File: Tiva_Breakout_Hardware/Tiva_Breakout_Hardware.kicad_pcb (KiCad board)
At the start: 2 copper layers, 139.8 x 79.5 mm, 11 parts, among them U1 TM4C129E_Launchpad

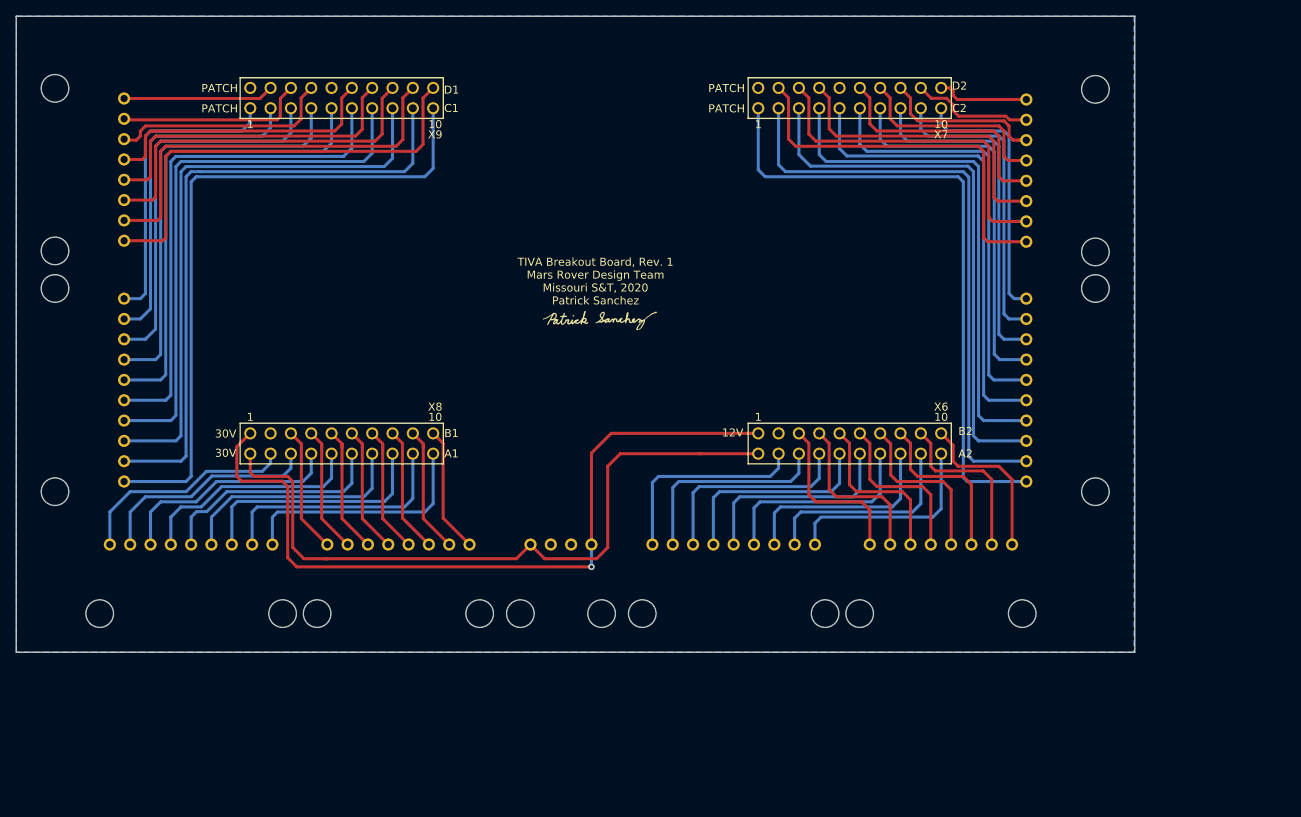
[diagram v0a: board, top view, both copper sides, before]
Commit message: rearranged pcb to account for physical layout
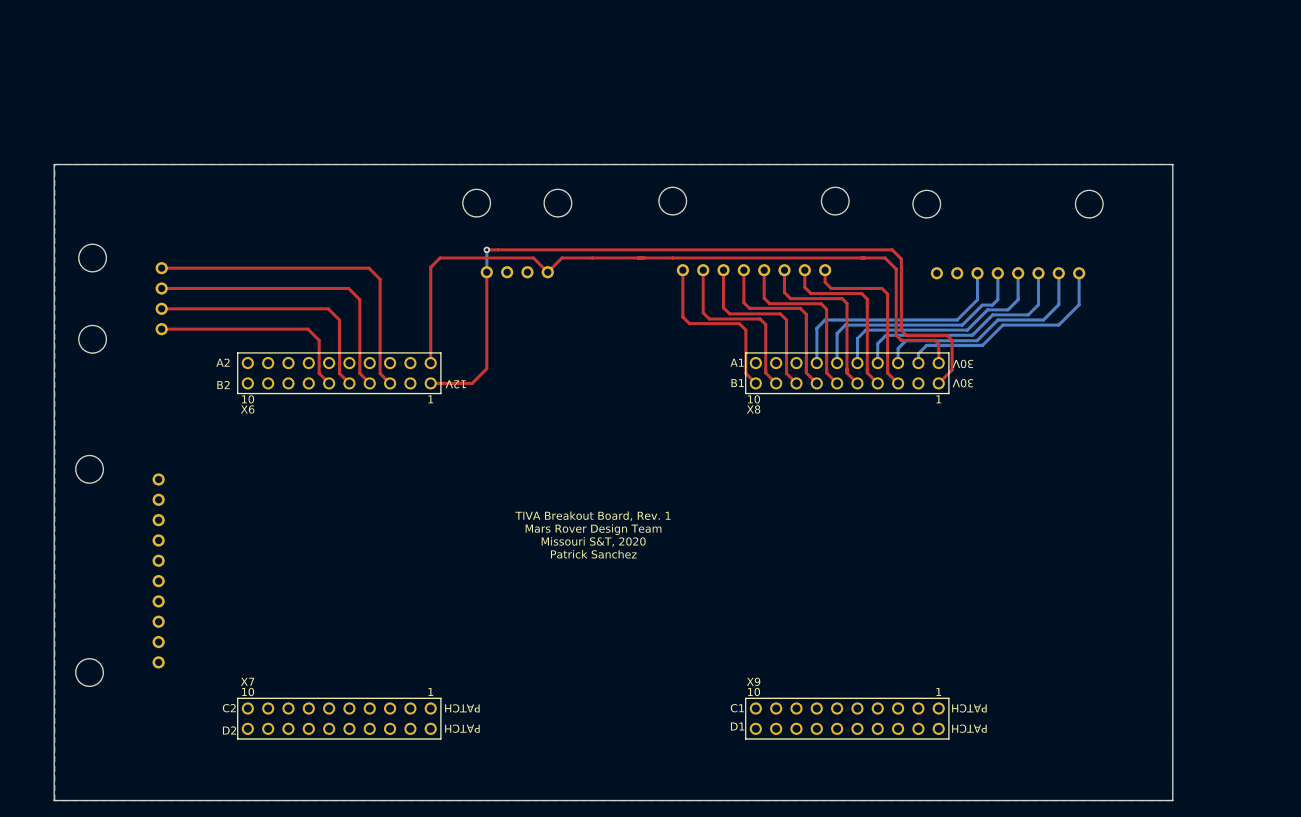
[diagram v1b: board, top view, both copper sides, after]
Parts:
- removed ConnA1, ConnA2: Molex_SL_09, MRDT_Connectors:MOLEX_SL_09_Horizontal
- removed ConnB1, ConnB2, ConnD1, ConnD2: Molex_SL_08, MRDT_Connectors:MOLEX_SL_08_Horizontal
- removed ConnC2: Molex_SL_10, MRDT_Connectors:MOLEX_SL_10_Horizontal
- removed G***: LOGO, MRDT_Silkscreens:z_sig_Patrick_Sanchez_15mmx5mm
- added 12V_B2: Molex_SL_04, MRDT_Connectors:MOLEX_SL_04_Horizontal, B.Cu at (90.3, 87.6)
- added Conn30V_L1: Molex_SL_08, MRDT_Connectors:MOLEX_SL_08_Horizontal, B.Cu at (196.1, 84.5)
- added Conn30V_R1: Molex_SL_08, MRDT_Connectors:MOLEX_SL_08_Horizontal, B.Cu at (164.3, 84.1)
- moved U1 89.7 mm to (188.7, 94.4), turned to 180 degrees
- moved ConnIN1 34.5 mm to (134.7, 84.3), turned to 180 degrees
- moved ConnPCH_C2 23.0 mm to (89.9, 121.7)
- renumbered ConnC1 to ConnPCH_C2
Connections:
- ConnPCH_C2 pad 1: Net-(ConnC1-Pad1) -> Net-(ConnPCH_C2-Pad1)
- ConnPCH_C2 pad 10: Net-(ConnC1-Pad10) -> Net-(ConnPCH_C2-Pad10)
- ConnPCH_C2 pad 2: Net-(ConnC1-Pad2) -> Net-(ConnPCH_C2-Pad2)
- ConnPCH_C2 pad 3: Net-(ConnC1-Pad3) -> Net-(ConnPCH_C2-Pad3)
- ConnPCH_C2 pad 4: Net-(ConnC1-Pad4) -> Net-(ConnPCH_C2-Pad4)
- ConnPCH_C2 pad 5: Net-(ConnC1-Pad5) -> Net-(ConnPCH_C2-Pad5)
- ConnPCH_C2 pad 6: Net-(ConnC1-Pad6) -> Net-(ConnPCH_C2-Pad6)
- ConnPCH_C2 pad 7: Net-(ConnC1-Pad7) -> Net-(ConnPCH_C2-Pad7)
- ConnPCH_C2 pad 8: Net-(ConnC1-Pad8) -> Net-(ConnPCH_C2-Pad8)
- ConnPCH_C2 pad 9: Net-(ConnC1-Pad9) -> Net-(ConnPCH_C2-Pad9)
- U1 pad PF1: Net-(ConnC1-Pad1) -> Net-(U1-PadPF1)
- U1 pad PF2: Net-(ConnC1-Pad2) -> Net-(U1-PadPF2)
- U1 pad PF3: Net-(ConnC1-Pad3) -> Net-(U1-PadPF3)
- U1 pad PG0: Net-(ConnC1-Pad4) -> Net-(U1-PadPG0)
- U1 pad PG1: Net-(ConnC2-Pad1) -> Net-(ConnPCH_C2-Pad1)
- U1 pad PH0: Net-(ConnC2-Pad7) -> Net-(ConnPCH_C2-Pad7)
- U1 pad PH1: Net-(ConnC2-Pad8) -> Net-(ConnPCH_C2-Pad8)
- U1 pad PK4: Net-(ConnC2-Pad2) -> Net-(ConnPCH_C2-Pad2)
- U1 pad PK5: Net-(ConnC2-Pad3) -> Net-(ConnPCH_C2-Pad3)
- U1 pad PK6: Net-(ConnC2-Pad9) -> Net-(ConnPCH_C2-Pad9)
- U1 pad PK7: Net-(ConnC2-Pad10) -> Net-(ConnPCH_C2-Pad10)
- U1 pad PL0: Net-(ConnC1-Pad7) -> Net-(U1-PadPL0)
- U1 pad PL1: Net-(ConnC1-Pad8) -> Net-(U1-PadPL1)
- U1 pad PL2: Net-(ConnC1-Pad9) -> Net-(U1-PadPL2)
- U1 pad PL3: Net-(ConnC1-Pad10) -> Net-(U1-PadPL3)
- U1 pad PL4: Net-(ConnC1-Pad5) -> Net-(U1-PadPL4)
- U1 pad PL5: Net-(ConnC1-Pad6) -> Net-(U1-PadPL5)
- U1 pad PM0: Net-(ConnC2-Pad4) -> Net-(ConnPCH_C2-Pad4)
- U1 pad PM1: Net-(ConnC2-Pad5) -> Net-(ConnPCH_C2-Pad5)
- U1 pad PM2: Net-(ConnC2-Pad6) -> Net-(ConnPCH_C2-Pad6)
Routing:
- net Net-(ConnC1-Pad10): track 83.9 -> 0.00 mm
- net Net-(ConnC1-Pad9): track 79.0 -> 0.00 mm
- net Net-(ConnC2-Pad1): track 79.0 -> 0.00 mm
- net Net-(ConnC2-Pad2): track 73.8 -> 0.00 mm
- net Net-(ConnC1-Pad8): track 73.8 -> 0.00 mm
- net Net-(ConnC1-Pad7): track 68.7 -> 0.00 mm
- net Net-(ConnC2-Pad3): track 68.4 -> 0.00 mm
- net Net-(ConnC2-Pad4): track 63.7 -> 0.00 mm
- net Net-(ConnC1-Pad6): track 63.6 -> 0.00 mm
- net Net-(ConnC1-Pad5): track 58.5 -> 0.00 mm
- net Net-(ConnC2-Pad5): track 58.5 -> 0.00 mm
- net Net-(U1-PadPP2): track 55.9 -> 0.00 mm
- net Net-(ConnC2-Pad6): track 53.5 -> 0.00 mm
- net Net-(ConnC1-Pad4): track 53.5 -> 0.00 mm
- net Net-(U1-PadPN3): track 50.8 -> 0.00 mm
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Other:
- board text removed: "PA4"
- board text removed: "PA5"
- board text removed: "PA6"
- board text removed: "PA7"
- board text removed: "PATCH PANEL"
- board text removed: "PB2"
- board text removed: "PB3"
- board text removed: "PC4"
- board text removed: "PC5"
- board text removed: "PC6"
- board text removed: "PC7"
- board text removed: "PD0"
- board text removed: "PD1"
- board text removed: "PD2"
- board text removed: "PD3"
- board text removed: "PD4"
- board text removed: "PD5"
- board text removed: "PD7"
- board text removed: "PE0"
- board text removed: "PE1"
- board text removed: "PE2"
- board text removed: "PE3"
- board text removed: "PE4"
- board text removed: "PE5"
- board text removed: "PF1"
- board text removed: "PF2"
- board text removed: "PF3"
- board text removed: "PG0"
- board text removed: "PG1"
- board text removed: "PH0"
- board text removed: "PH1"
- board text removed: "PH2"
- board text removed: "PH3"
- board text removed: "PK2"
- board text removed: "PK3"
- board text removed: "PK4"
- board text removed: "PK5"
- board text removed: "PK6"
- board text removed: "PK7"
- board text removed: "PL0"
- board text removed: "PL1"
- board text removed: "PL2"
- board text removed: "PL3"
- board text removed: "PL4"
- board text removed: "PL5"
- board text removed: "PM0"
- board text removed: "PM1"
- board text removed: "PM2"
- board text removed: "PM3"
- board text removed: "PM4"
- board text removed: "PM5"
- board text removed: "PM6"
- board text removed: "PM7"
- board text removed: "PN2"
- board text removed: "PN3"
- board text removed: "PN4"
- board text removed: "PN5"
- board text removed: "PP0"
- board text removed: "PP1"
- board text removed: "PP2"
- board text removed: "PP3"
- board text removed: "PP4"
- board text removed: "PP5"
- board text removed: "PQ0"
- board text removed: "PQ1"
- board text removed: "PQ2"
- board text removed: "PQ3"

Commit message: In process of changing layout for smaller board
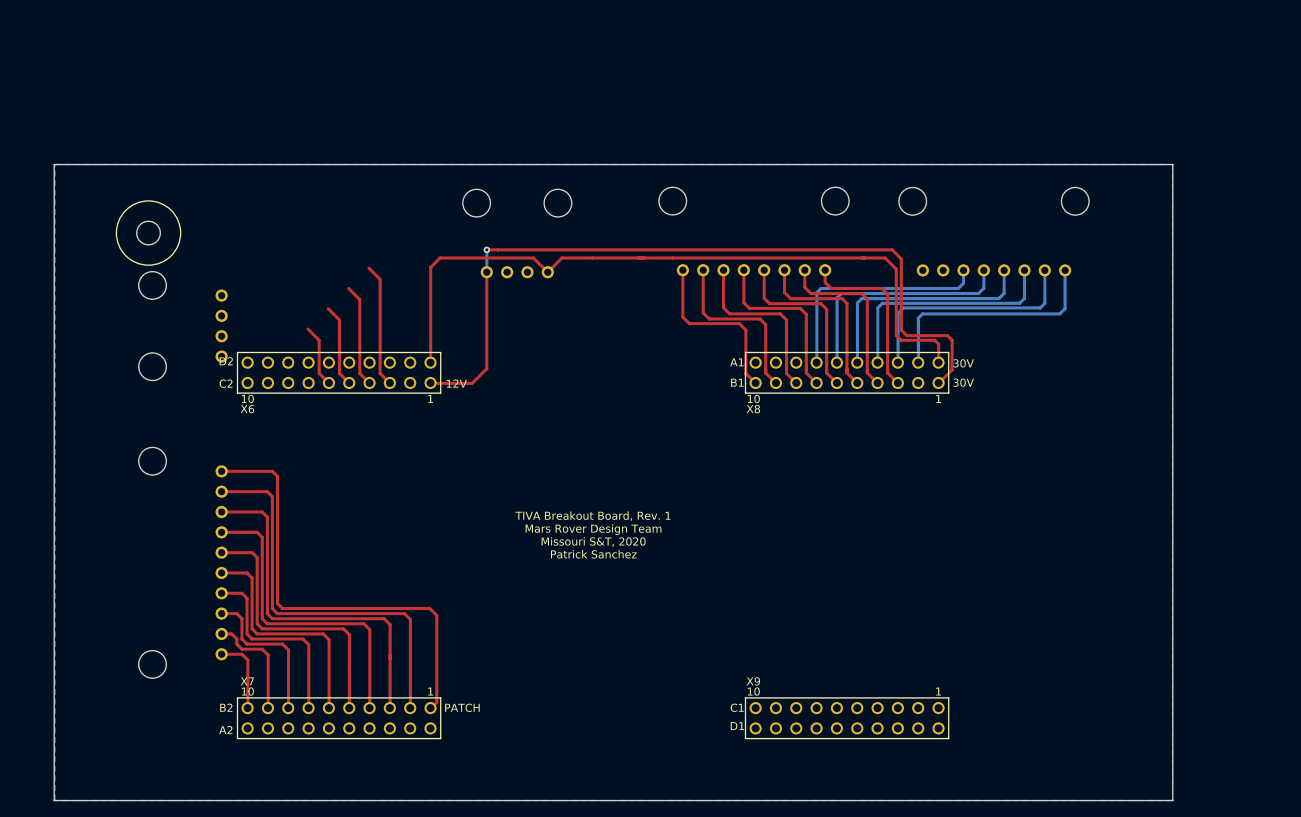
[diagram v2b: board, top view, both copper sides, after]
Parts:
- added REF**: 4_40_Hole, MRDT_Drill_Holes:4_40_Hole_Corner, F.Cu at (92.7, 83.4)
- moved U1 89.2 mm to (107.4, 131.2), turned to 0 degrees
- moved 12V_B2 8.24 mm to (97.8, 91.1)
- moved ConnPCH_C2 7.94 mm to (97.8, 120.7)
- moved Conn30V_L1 1.79 mm to (194.3, 84.1)
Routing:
- net Net-(ConnPCH_C2-Pad1): track 0.00 -> 55.6 mm
- net Net-(ConnPCH_C2-Pad2): track 0.00 -> 49.5 mm
- net Net-(ConnPCH_C2-Pad3): track 0.00 -> 44.9 mm
- net Net-(ConnPCH_C2-Pad4): track 0.00 -> 39.4 mm
- net Net-(ConnPCH_C2-Pad5): track 0.00 -> 34.3 mm
- net Net-(ConnPCH_C2-Pad6): track 0.00 -> 29.2 mm
- net Net-(12V_B2-Pad1): track 41.4 -> 15.5 mm
- net Net-(ConnPCH_C2-Pad7): track 0.00 -> 24.1 mm
- net Net-(12V_B2-Pad2): track 36.3 -> 13.0 mm
- net Net-(12V_B2-Pad3): track 31.5 -> 10.7 mm
- net Net-(ConnPCH_C2-Pad8): track 0.00 -> 19.0 mm
- net Net-(12V_B2-Pad4): track 26.2 -> 7.88 mm
- net Net-(ConnPCH_C2-Pad9): track 0.00 -> 14.0 mm
- net Net-(ConnPCH_C2-Pad10): track 0.00 -> 9.63 mm
- net Net-(Conn30V_L1-Pad1): track 27.9 -> 29.2 mm
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
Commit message: In process of rearranging for new layout
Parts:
- moved 12V_B2 7.50 mm to (104.9, 88.5), turned to 180 degrees
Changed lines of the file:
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@@
   )
   (setup
-    (last_trace_width 0.381)
+    (last_trace_width 0.25)
     (user_trace_width 0.254)
     (user_trace_width 0.381)
@@
     (add_net "Net-(U1-PadRese')")
     (add_net "Net-(U1-PadRese)")
+  )
+  (module MRDT_Connectors:MOLEX_SL_08_Horizontal (layer B.Cu)
+    (at 164.338 84.074 180)
+    (fp_text reference Conn30V_R1 (at -7.62 -2.54) (layer B.SilkS) hide
+      (effects (font (size 1 1) (thickness 0.15)) (justify mirror))
+    )
+    (fp_text value Molex_SL_08 (at 0 -2.54) (layer B.Fab)
+      (effects (font (size 1 1) (thickness 0.15)) (justify mirror))
+    )
+    (fp_line (start -10.16 -1.27) (end -10.16 1.27) (layer B.SilkS) (width 0.15))
+    (fp_line (start 10.16 -1.27) (end -10.16 -1.27) (layer B.SilkS) (width 0.15))
+    (fp_line (start 10.16 1.27) (end 10.16 -1.27) (layer B.SilkS) (width 0.15))
+    (fp_line (start 1.27 5.08) (end 1.27 7.62) (layer B.SilkS) (width 0.15))
+    (fp_line (start -1.27 5.08) (end 1.27 5.08) (layer B.SilkS) (width 0.15))
+    (fp_line (start -1.27 7.62) (end -1.27 5.08) (layer B.SilkS) (width 0.15))
+    (fp_line (start -7.62 8.89) (end -7.62 12.7) (layer B.SilkS) (width 0.15))
+    (fp_line (start 7.62 7.62) (end 7.62 13.208) (layer B.SilkS) (width 0.15))
+    (fp_line (start -7.62 7.62) (end 7.62 7.62) (layer B.SilkS) (width 0.15))
+    (fp_line (start -7.62 8.89) (end -7.62 7.62) (layer B.SilkS) (width 0.15))
+    (fp_line (start -12.06 1.27) (end -12.065 1.27) (layer B.SilkS) (width 0.15))
+    (fp_line (start 12.065 1.27) (end 12.065 13.208) (layer B.SilkS) (width 0.15))
+    (fp_line (start -12.065 1.27) (end -12.065 13.208) (layer B.SilkS) (width 0.15))
+    (fp_line (start -12.065 13.208) (end 12.065 13.208) (layer B.SilkS) (width 0.15))
+    (fp_line (start -7.62 13.208) (end -7.62 12.7) (layer B.SilkS) (width 0.15))
+    (fp_line (start -12.065 1.27) (end 12.065 1.27) (layer B.SilkS) (width 0.15))
+    (pad 8 thru_hole circle (at 8.89 0 180) (size 1.524 1.524) (drill 0.9) (layers *.Cu *.Mask)
+      (net 18 "Net-(Conn30V_R1-Pad8)"))
+    (pad 7 thru_hole circle (at 6.35 0 180) (size 1.524 1.524) (drill 0.9) (layers *.Cu *.Mask)
+      (net 19 "Net-(Conn30V_R1-Pad7)"))
+    (pad 6 thru_hole circle (at 3.81 0 180) (size 1.524 1.524) (drill 0.9) (layers *.Cu *.Mask)
+      (net 20 "Net-(Conn30V_R1-Pad6)"))
+    (pad "" np_thru_hole circle (at 10.16 8.636 180) (size 3.45 3.45) (drill 3.45) (layers *.Cu *.Mask))
+    (pad "" np_thru_hole circle (at -10.16 8.636 180) (size 3.45 3.45) (drill 3.45) (layers *.Cu *.Mask))
+    (pad 5 thru_hole circle (at 1.27 0 180) (size 1.524 1.524) (drill 0.9) (layers *.Cu *.Mask)
+      (net 21 "Net-(Conn30V_R1-Pad5)"))
+    (pad 4 thru_hole circle (at -1.27 0 180) (size 1.524 1.524) (drill 0.9) (layers *.Cu *.Mask)
+      (net 22 "Net-(Conn30V_R1-Pad4)"))
+    (pad 3 thru_hole circle (at -3.81 0 180) (size 1.524 1.524) (drill 0.9) (layers *.Cu *.Mask)
+      (net 23 "Net-(Conn30V_R1-Pad3)"))
+    (pad 2 thru_hole circle (at -6.35 0 180) (size 1.524 1.524) (drill 0.9) (layers *.Cu *.Mask)
+      (net 24 "Net-(Conn30V_R1-Pad2)"))
+    (pad 1 thru_hole circle (at -8.89 0 180) (size 1.524 1.524) (drill 0.9) (layers *.Cu *.Mask)
+      (net 25 "Net-(Conn30V_R1-Pad1)"))
+    (model "${MRDT_KICAD_LIBRARIES}/3D Files/MRDT_Connctors/Molex_SL_08_Horizontal.stp"
+      (offset (xyz 11.42999982833862 12.95399980545044 0))
+      (scale (xyz 1 1 1))
+      (rotate (xyz 0 0 180))
+    )
   )
   (module MRDT_Drill_Holes:4_40_Hole_Corner (layer F.Cu)
@@
   )
   (module MRDT_Connectors:MOLEX_SL_04_Horizontal (layer B.Cu)
-    (at 97.79 91.059 270)
-    (fp_text reference 12V_B2 (at -2.54 -2.54 90) (layer B.SilkS) hide
-      (effects (font (size 1 1) (thickness 0.15)) (justify mirror))
-    )
-    (fp_text value Molex_SL_04 (at -0.635 -2.032 90) (layer B.Fab)
+    (at 104.8512 88.519 180)
+    (fp_text reference 12V_B2 (at -2.54 -2.54) (layer B.SilkS) hide
+      (effects (font (size 1 1) (thickness 0.15)) (justify mirror))
+    )
+    (fp_text value Molex_SL_04 (at -0.635 -2.032) (layer B.Fab)
       (effects (font (size 1 1) (thickness 0.15)) (justify mirror))
     )
@@
     (fp_line (start 5.08 1.27) (end 5.08 -1.27) (layer B.SilkS) (width 0.15))
     (fp_line (start -5.08 -1.27) (end -5.08 1.27) (layer B.SilkS) (width 0.15))
-    (pad 1 thru_hole circle (at -3.81 0 270) (size 1.524 1.524) (drill 0.9) (layers *.Cu *.Mask)
+    (pad 1 thru_hole circle (at -3.81 0 180) (size 1.524 1.524) (drill 0.9) (layers *.Cu *.Mask)
       (net 6 "Net-(12V_B2-Pad1)"))
-    (pad 2 thru_hole circle (at -1.27 0 270) (size 1.524 1.524) (drill 0.9) (layers *.Cu *.Mask)
+    (pad 2 thru_hole circle (at -1.27 0 180) (size 1.524 1.524) (drill 0.9) (layers *.Cu *.Mask)
       (net 7 "Net-(12V_B2-Pad2)"))
-    (pad 3 thru_hole circle (at 1.27 0 270) (size 1.524 1.524) (drill 0.9) (layers *.Cu *.Mask)
+    (pad 3 thru_hole circle (at 1.27 0 180) (size 1.524 1.524) (drill 0.9) (layers *.Cu *.Mask)
       (net 8 "Net-(12V_B2-Pad3)"))
-    (pad 4 thru_hole circle (at 3.81 0 270) (size 1.524 1.524) (drill 0.9) (layers *.Cu *.Mask)
+    (pad 4 thru_hole circle (at 3.81 0 180) (size 1.524 1.524) (drill 0.9) (layers *.Cu *.Mask)
       (net 9 "Net-(12V_B2-Pad4)"))
-    (pad "" np_thru_hole circle (at -5.08 8.636 270) (size 3.45 3.45) (drill 3.45) (layers *.Cu *.Mask))
-    (pad "" np_thru_hole circle (at 5.08 8.636 270) (size 3.45 3.45) (drill 3.45) (layers *.Cu *.Mask))
+    (pad "" np_thru_hole circle (at -5.08 8.636 180) (size 3.45 3.45) (drill 3.45) (layers *.Cu *.Mask))
+    (pad "" np_thru_hole circle (at 5.08 8.636 180) (size 3.45 3.45) (drill 3.45) (layers *.Cu *.Mask))
     (model "${MRDT_KICAD_LIBRARIES}/3D Files/MRDT_Connctors/Molex_SL_04_Horizontal.stp"
       (offset (xyz 6.349999904632568 12.95399980545044 0))
@@
     (model "${MRDT_KICAD_LIBRARIES}/3D Files/MRDT_Connctors/Molex_SL_08_Horizontal.stp"
       (offset (xyz 11.42999982833862 12.95399980545044 0))
-      (scale (xyz 1 1 1))
-      (rotate (xyz 0 0 180))
-    )
-  )
-  (module MRDT_Connectors:MOLEX_SL_08_Horizontal (layer B.Cu)
-    (at 164.338 84.074 180)
-    (fp_text reference Conn30V_R1 (at -7.62 -2.54) (layer B.SilkS) hide
-      (effects (font (size 1 1) (thickness 0.15)) (justify mirror))
-    )
-    (fp_text value Molex_SL_08 (at 0 -2.54) (layer B.Fab)
-      (effects (font (size 1 1) (thickness 0.15)) (justify mirror))
-    )
-    (fp_line (start -10.16 -1.27) (end -10.16 1.27) (layer B.SilkS) (width 0.15))
-    (fp_line (start 10.16 -1.27) (end -10.16 -1.27) (layer B.SilkS) (width 0.15))
-    (fp_line (start 10.16 1.27) (end 10.16 -1.27) (layer B.SilkS) (width 0.15))
-    (fp_line (start 1.27 5.08) (end 1.27 7.62) (layer B.SilkS) (width 0.15))
-    (fp_line (start -1.27 5.08) (end 1.27 5.08) (layer B.SilkS) (width 0.15))
-    (fp_line (start -1.27 7.62) (end -1.27 5.08) (layer B.SilkS) (width 0.15))
-    (fp_line (start -7.62 8.89) (end -7.62 12.7) (layer B.SilkS) (width 0.15))
-    (fp_line (start 7.62 7.62) (end 7.62 13.208) (layer B.SilkS) (width 0.15))
-    (fp_line (start -7.62 7.62) (end 7.62 7.62) (layer B.SilkS) (width 0.15))
-    (fp_line (start -7.62 8.89) (end -7.62 7.62) (layer B.SilkS) (width 0.15))
-    (fp_line (start -12.06 1.27) (end -12.065 1.27) (layer B.SilkS) (width 0.15))
-    (fp_line (start 12.065 1.27) (end 12.065 13.208) (layer B.SilkS) (width 0.15))
-    (fp_line (start -12.065 1.27) (end -12.065 13.208) (layer B.SilkS) (width 0.15))
-    (fp_line (start -12.065 13.208) (end 12.065 13.208) (layer B.SilkS) (width 0.15))
-    (fp_line (start -7.62 13.208) (end -7.62 12.7) (layer B.SilkS) (width 0.15))
-    (fp_line (start -12.065 1.27) (end 12.065 1.27) (layer B.SilkS) (width 0.15))
-    (pad 8 thru_hole circle (at 8.89 0 180) (size 1.524 1.524) (drill 0.9) (layers *.Cu *.Mask)
-      (net 18 "Net-(Conn30V_R1-Pad8)"))
-    (pad 7 thru_hole circle (at 6.35 0 180) (size 1.524 1.524) (drill 0.9) (layers *.Cu *.Mask)
-      (net 19 "Net-(Conn30V_R1-Pad7)"))
-    (pad 6 thru_hole circle (at 3.81 0 180) (size 1.524 1.524) (drill 0.9) (layers *.Cu *.Mask)
-      (net 20 "Net-(Conn30V_R1-Pad6)"))
-    (pad "" np_thru_hole circle (at 10.16 8.636 180) (size 3.45 3.45) (drill 3.45) (layers *.Cu *.Mask))
-    (pad "" np_thru_hole circle (at -10.16 8.636 180) (size 3.45 3.45) (drill 3.45) (layers *.Cu *.Mask))
-    (pad 5 thru_hole circle (at 1.27 0 180) (size 1.524 1.524) (drill 0.9) (layers *.Cu *.Mask)
-      (net 21 "Net-(Conn30V_R1-Pad5)"))
-    (pad 4 thru_hole circle (at -1.27 0 180) (size 1.524 1.524) (drill 0.9) (layers *.Cu *.Mask)
-      (net 22 "Net-(Conn30V_R1-Pad4)"))
-    (pad 3 thru_hole circle (at -3.81 0 180) (size 1.524 1.524) (drill 0.9) (layers *.Cu *.Mask)
-      (net 23 "Net-(Conn30V_R1-Pad3)"))
-    (pad 2 thru_hole circle (at -6.35 0 180) (size 1.524 1.524) (drill 0.9) (layers *.Cu *.Mask)
-      (net 24 "Net-(Conn30V_R1-Pad2)"))
-    (pad 1 thru_hole circle (at -8.89 0 180) (size 1.524 1.524) (drill 0.9) (layers *.Cu *.Mask)
-      (net 25 "Net-(Conn30V_R1-Pad1)"))
-    (model "${MRDT_KICAD_LIBRARIES}/3D Files/MRDT_Connctors/Molex_SL_08_Horizontal.stp"
-      (offset (xyz 11.42999982833862 12.95399980545044 0))
